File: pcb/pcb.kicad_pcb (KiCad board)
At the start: 2 copper layers, 229.9 x 97.8 mm, 154 parts, among them J1 USB_C_Receptacle_USB2.0, SW1 Reset, SW10 SW_Push, SW11 SW_Push, SW12 SW_Push, SW13 SW_Push, SW14 SW_Push, SW15 SW_Push, SW16 SW_Push, SW17 SW_Push, SW18 SW_Push, SW19 SW_Push, SW2 SW_Push, SW20 SW_Push, SW21 SW_Push, SW22 SW_Push, SW23 SW_Push, SW24 SW_Push, SW25 SW_Push, SW26 SW_Push, SW27 SW_Push, SW28 SW_Push, SW29 SW_Push, SW3 SW_Push, SW30 SW_Push, SW31 SW_Push, SW32 SW_Push, SW33 SW_Push, SW34 SW_Push, SW35 SW_Push, SW36 SW_Push, SW37 SW_Push, SW38 SW_Push, SW39 SW_Push, SW4 SW_Push, SW40 SW_Push, SW41 SW_Push, SW42 SW_Push, SW43 SW_Push, SW44 SW_Push, SW45 SW_Push, SW46 SW_Push, SW47 SW_Push, SW48 SW_Push, SW49 SW_Push, SW5 SW_Push, SW50 SW_Push, SW51 SW_Push, SW52 SW_Push, SW53 SW_Push, SW54 SW_Push, SW55 SW_Push, SW56 SW_Push, SW57 SW_Push, SW58 SW_Push, SW59 SW_Push, SW6 SW_Push, SW60 SW_Push, SW7 SW_Push, SW8 SW_Push, SW9 SW_Push, U1 ATmega32U4-AU, Y1 TSX3225

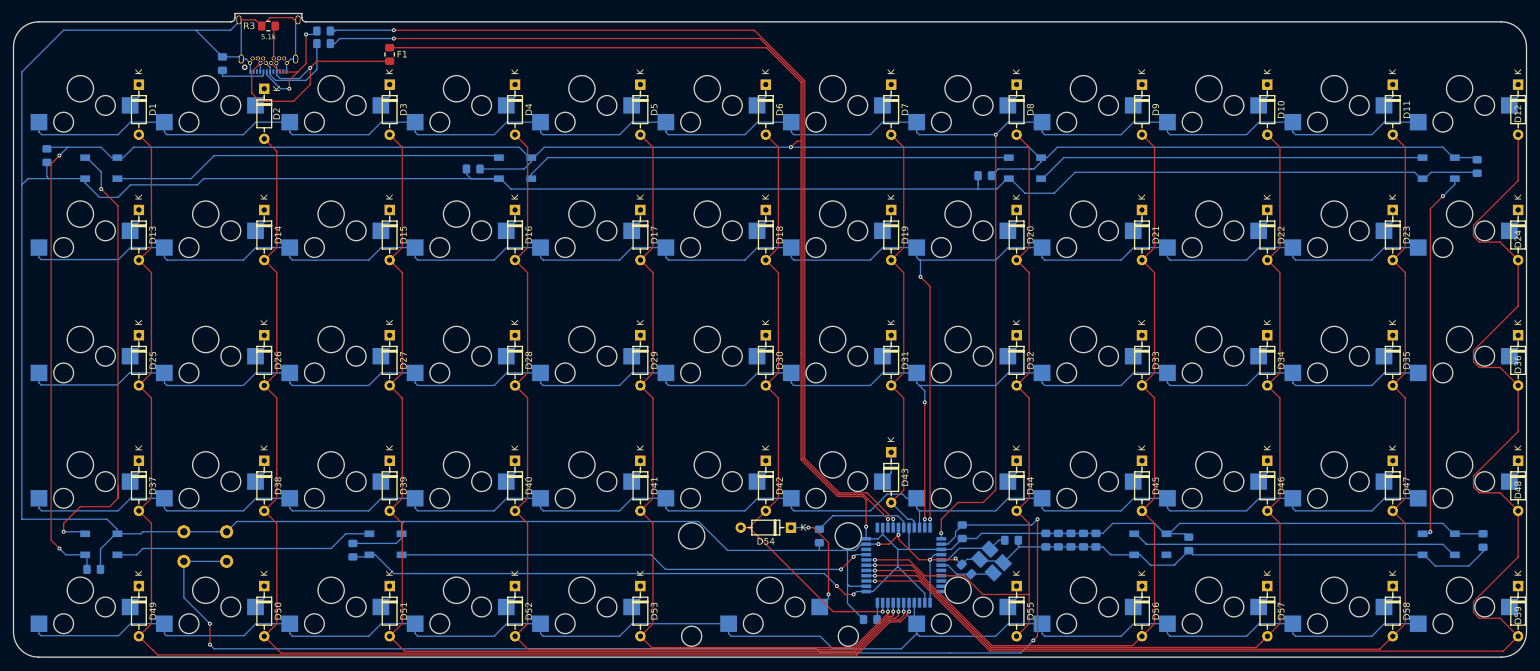
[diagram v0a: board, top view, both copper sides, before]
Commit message: Finish PCB design, generate gerber files
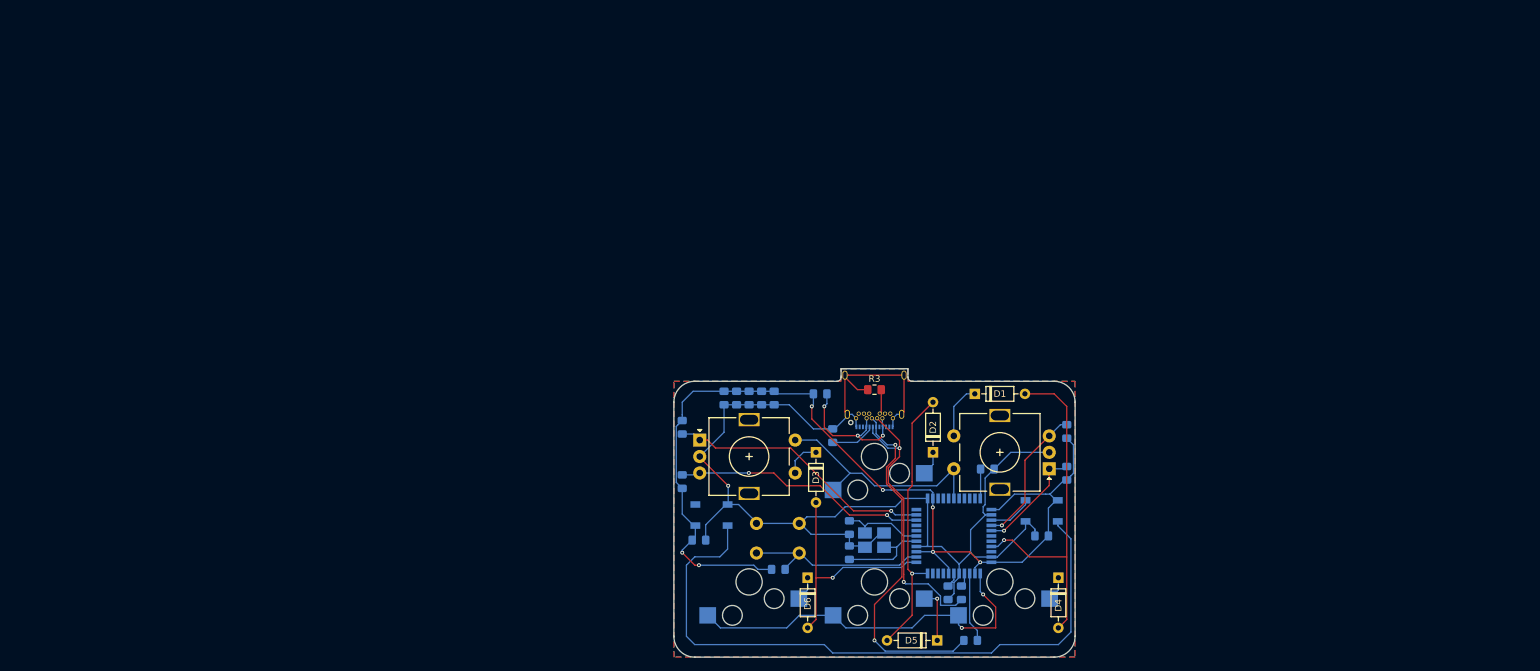
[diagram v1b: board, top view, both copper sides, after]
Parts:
- removed C11, C12, C13, C14, C15, C16: 100nF, Capacitor_SMD:C_0805_2012Metric_Pad1.15x1.40mm_HandSolder
- removed D10, D11, D12, D13, D14, D15, D16, D17, D18, D19, D20, D21, D22, D23, D24, D25, D26, D27, D28, D29, D30, D31, D32, D33, D34, D35, D36, D37, D38, D39, D40, D41, D42, D43, D44, D45, D46, D47, D48, D49, D50, D51, D52, D53, D54, D55, D56, D57, D58, D59, D9: 1N4148, Diode_THT:D_DO-35_SOD27_P7.62mm_Horizontal
- removed D60, D61, D62, D63, D64, D65, D66, D67: WS2812B, LED_SMD:LED_WS2812B_PLCC4_5.0x5.0mm_P3.2mm
- removed REF**: SW_Stabilizer, keyswitches:MX_Stabilizer_2u
- removed SW1: Reset, Button_Switch_THT:SW_PUSH_6mm
- removed SW10, SW11, SW12, SW13, SW14, SW15, SW16, SW17, SW18, SW19, SW20, SW21, SW22, SW23, SW24, SW25, SW26, SW27, SW28, SW29, SW30, SW31, SW32, SW33, SW34, SW35, SW36, SW37, SW38, SW39, SW40, SW41, SW42, SW43, SW44, SW45, SW46, SW47, SW48, SW49, SW50, SW51, SW52, SW53, SW54, SW55, SW56, SW57, SW58, SW59, SW60, SW8, SW9: SW_Push, keyswitches:Kailh_socket_plate_mount
- added R10: 10k, Resistor_SMD:R_0805_2012Metric_Pad1.15x1.40mm_HandSolder, B.Cu at (129.5, 90.8)
- added R7: 10k, Resistor_SMD:R_0805_2012Metric_Pad1.15x1.40mm_HandSolder, B.Cu at (188.0, 91.4)
- added R8: 10k, Resistor_SMD:R_0805_2012Metric_Pad1.15x1.40mm_HandSolder, B.Cu at (188.0, 97.8)
- added R9: 10k, Resistor_SMD:R_0805_2012Metric_Pad1.15x1.40mm_HandSolder, B.Cu at (129.5, 99.1)
- added Reset: Reset, Button_Switch_THT:SW_PUSH_6mm, B.Cu at (147.3, 105.4)
- D7, D8: value 1N4148 -> WS2812B; footprint Diode_THT:D_DO-35_SOD27_P7.62mm_Horizontal -> LED_SMD:LED_WS2812B_PLCC4_5.0x5.0mm_P3.2mm; moved to B.Cu
- F1: moved to B.Cu
- SW2, SW3: value SW_Push -> EC11; footprint keyswitches:Kailh_socket_plate_mount -> Rotary_Encoder:RotaryEncoder_Alps_EC11E-Switch_Vertical_H20mm
- moved SW2 158.1 mm to (185.3, 97.1)
- moved D1 135.4 mm to (174.0, 85.7), turned to 0 degrees
- moved R5 133.7 mm to (173.4, 123.2)
- moved R4 129.1 mm to (172.0, 116.0), turned to 270 degrees
- moved D2 115.6 mm to (167.6, 94.6), turned to 90 degrees
- moved SW5 111.5 mm to (177.8, 114.3)
- moved D4 111.5 mm to (186.7, 113.7)
- moved R2 108.6 mm to (152.4, 92.1)
- moved R3 107.4 mm to (158.8, 85.1)
- moved J1 106.7 mm to (158.8, 85.7)
- moved C9 104.7 mm to (184.2, 107.3), turned to 180 degrees
- moved SW4 99.7 mm to (158.8, 95.2)
- moved D5 95.7 mm to (168.3, 123.2), turned to 180 degrees
- moved SW3 92.1 mm to (132.2, 92.8), turned to 0 degrees
- moved C10 92.1 mm to (132.1, 108.0)
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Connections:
- D4 pad 2: col3 -> col0
- D5 pad 2: col4 -> col1
- D6 pad 2: col5 -> col2
- D7 pad 1: Net-(D7-Pad1) -> VCC
- D7 pad 2: col6 -> Net-(D7-Pad2)
- D8 pad 1: Net-(D8-Pad1) -> VCC
- D8 pad 2: col7 -> Net-(D8-Pad2)
- SW4 pad 2: Net-(D3-Pad1) -> Net-(D2-Pad1)
- SW5 pad 1: row0 -> row1
- SW6 pad 1: row0 -> row1
- SW7 pad 1: row0 -> row1
- U1 pad 1: Net-(U1-Pad1) -> row1
- U1 pad 10: row2 -> Net-(U1-Pad10)
- U1 pad 11: row1 -> col1
- U1 pad 12: row0 -> col2
- U1 pad 20: Net-(U1-Pad20) -> R2B
- U1 pad 21: Net-(U1-Pad21) -> R2A
- U1 pad 26: row4 -> Net-(U1-Pad26)
- U1 pad 27: col0 -> Net-(U1-Pad27)
- U1 pad 28: col1 -> row0
- U1 pad 29: col2 -> Net-(U1-Pad29)
- U1 pad 30: col3 -> Net-(U1-Pad30)
- U1 pad 31: col4 -> Net-(U1-Pad31)
- U1 pad 32: col5 -> Net-(U1-Pad32)
- U1 pad 36: col11 -> led0
- U1 pad 37: col10 -> R1B
- U1 pad 38: col9 -> R1A
- U1 pad 39: col8 -> Net-(U1-Pad39)
- U1 pad 40: col7 -> Net-(U1-Pad40)
- U1 pad 41: led0 -> col0
- U1 pad 8: col6 -> Net-(U1-Pad8)
- U1 pad 9: row3 -> Net-(U1-Pad9)
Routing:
- net VCC: track 655.2 -> 153.4 mm, vias 6 -> 7
- net GND: track 659.3 -> 191.0 mm, vias 4 -> 1
- net row0: track 303.6 -> 36.2 mm, vias 2 -> 0
- net row2: track 258.5 -> 0.00 mm, vias 2 -> 0
- net row3: track 240.5 -> 0.00 mm
- net row4: track 238.9 -> 0.00 mm
- net row1: track 277.8 -> 57.8 mm
- net col11: track 210.5 -> 0.00 mm, vias 1 -> 0
- net col10: track 168.0 -> 0.00 mm, vias 1 -> 0
- net Net-(R1-Pad1): track 182.5 -> 28.9 mm, vias 4 -> 0
- net col0: track 204.9 -> 54.2 mm
- net Net-(R4-Pad1): track 151.3 -> 2.19 mm, vias 2 -> 0
- net col9: track 149.0 -> 0.00 mm, vias 1 -> 0
- net col3: track 144.9 -> 0.00 mm, vias 1 -> 0
- net col1: track 184.4 -> 42.4 mm
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- added copper zone on B.Cu, net GND
- added copper zone on F.Cu, net GND
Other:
- board size 229.9 x 97.8 mm -> 61 x 43.8 mm
- board text added: "Pulse 4k"
- board text removed: "Phoebe Keyboard"
- board text removed: "·"
